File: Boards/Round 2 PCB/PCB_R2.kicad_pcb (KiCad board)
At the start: 2 copper layers, 97 x 89.5 mm, 67 parts, among them J1 Screw_Terminal_01x12, J10 Screw_Terminal_01x03, J11 Screw_Terminal_01x12, J12 Screw_Terminal_01x03, J13 Screw_Terminal_01x03, J14 Screw_Terminal_01x03, J15 Screw_Terminal_01x03, J16 Screw_Terminal_01x03, J17 Screw_Terminal_01x03, J18 Screw_Terminal_01x03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

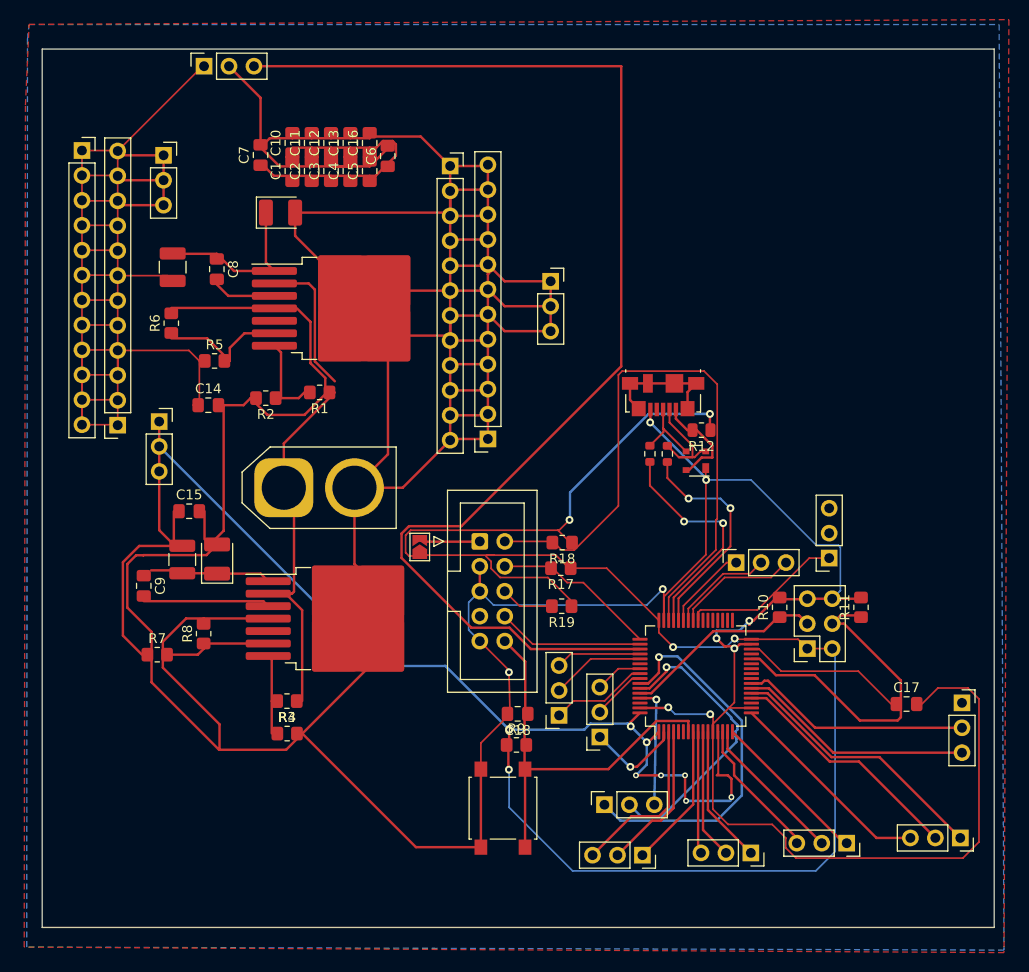
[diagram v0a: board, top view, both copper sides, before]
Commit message: ground layer test
placed all transistors, about to delete all ground connections
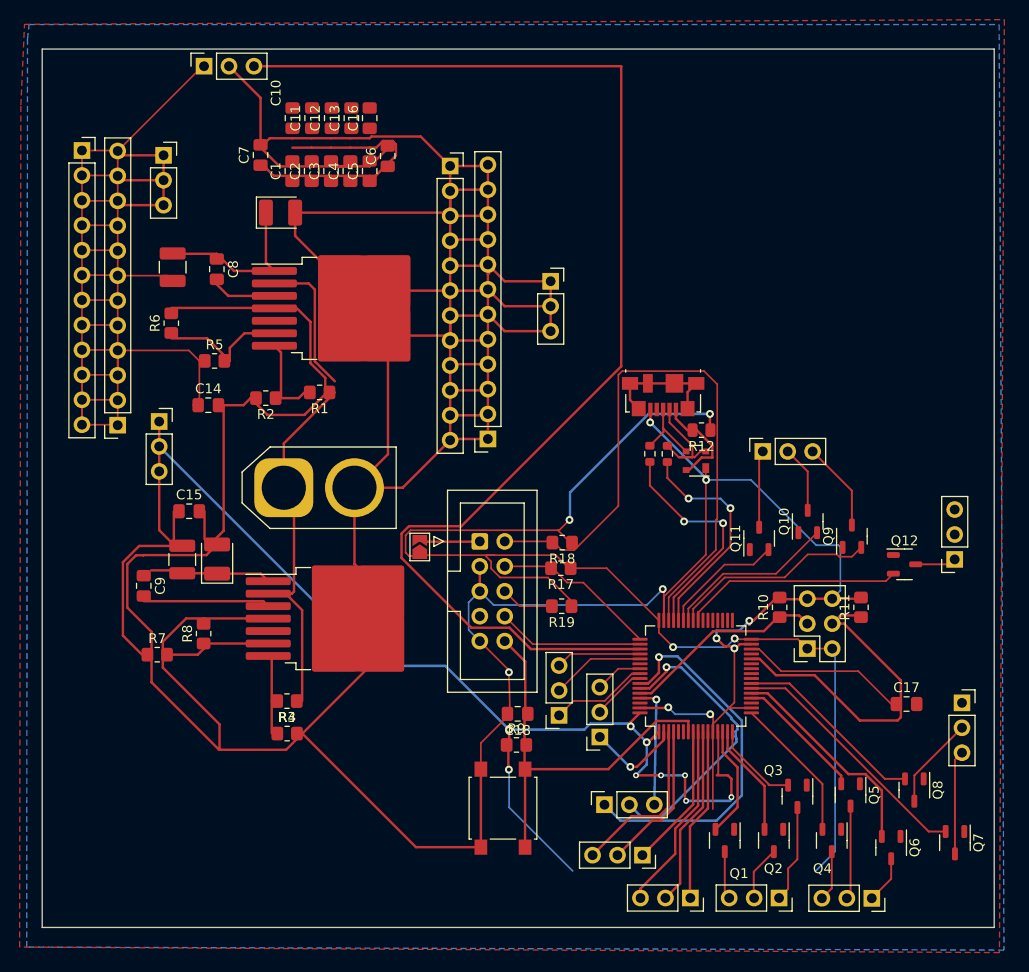
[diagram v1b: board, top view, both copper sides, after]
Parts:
- added Q1: NMOS, Package_TO_SOT_SMD:SOT-23-3, F.Cu at (121.5, 111.6)
- added Q10: NMOS, Package_TO_SOT_SMD:SOT-23-3, F.Cu at (130.0, 79.1)
- added Q11: NMOS, Package_TO_SOT_SMD:SOT-23-3, F.Cu at (125.0, 80.9)
- added Q12: NMOS, Package_TO_SOT_SMD:SOT-23-3, F.Cu at (139.9, 83.5)
- added Q2: NMOS, Package_TO_SOT_SMD:SOT-23-3, F.Cu at (126.5, 111.6)
- added Q3: NMOS, Package_TO_SOT_SMD:SOT-23-3, F.Cu at (128.9, 107.1)
- added Q4: NMOS, Package_TO_SOT_SMD:SOT-23-3, F.Cu at (132.4, 111.6)
- added Q5: NMOS, Package_TO_SOT_SMD:SOT-23-3, F.Cu at (134.4, 107.0)
- added Q6: NMOS, Package_TO_SOT_SMD:SOT-23-3, F.Cu at (138.5, 112.4)
- added Q7: NMOS, Package_TO_SOT_SMD:SOT-23-3, F.Cu at (145.0, 111.9)
- added Q8: NMOS, Package_TO_SOT_SMD:SOT-23-3, F.Cu at (140.9, 106.5)
- added Q9: NMOS, Package_TO_SOT_SMD:SOT-23-3, F.Cu at (134.5, 80.6)
- moved J15 12.8 mm to (145.0, 83.0)
- moved J10 11.6 mm to (125.4, 72.0)
- moved J13 10.9 mm to (136.5, 117.5)
- moved J12 8.87 mm to (127.1, 117.5)
- moved J19 7.69 mm to (118.0, 117.5)
- moved C13 2.53 mm to (83.5, 38.0)
- moved C12 2.53 mm to (81.5, 38.0)
- moved C11 2.53 mm to (79.5, 38.0)
- moved C10 2.53 mm to (77.5, 38.0)
- moved C16 2.53 mm to (85.4, 38.0)
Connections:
- U1 pad 14: /M0 -> /T0
- U1 pad 15: /M1 -> /T1
- U1 pad 16: /M2 -> /T2
- U1 pad 17: /M3 -> /T3
- U1 pad 20: /M4 -> /T4
- U1 pad 21: /M5 -> /T5
- U1 pad 22: /M6 -> /T6
- U1 pad 23: /M7 -> /T7
- U1 pad 40: /M11 -> /T11
- U1 pad 41: /M8 -> /T8
- U1 pad 42: /M9 -> /T9
- U1 pad 43: /M10 -> /T10
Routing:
- net GND: track 614.6 -> 562.6 mm
- net /T6: track 0.00 -> 25.8 mm
- net +3.3V: track 294.6 -> 269.8 mm
- net /T11: track 0.00 -> 24.0 mm
- net /M5: track 27.4 -> 4.84 mm
- net /T5: track 0.00 -> 22.1 mm
- net /T8: track 0.00 -> 21.1 mm
- net /T7: track 0.00 -> 19.7 mm
- net /T9: track 0.00 -> 17.5 mm
- net /M3: track 21.5 -> 5.17 mm
- net /M4: track 24.6 -> 9.54 mm
- net /M7: track 24.5 -> 9.49 mm
- net /T3: track 0.00 -> 14.9 mm
- net /M6: track 24.2 -> 10.6 mm
- net /T4: track 0.00 -> 13.2 mm
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
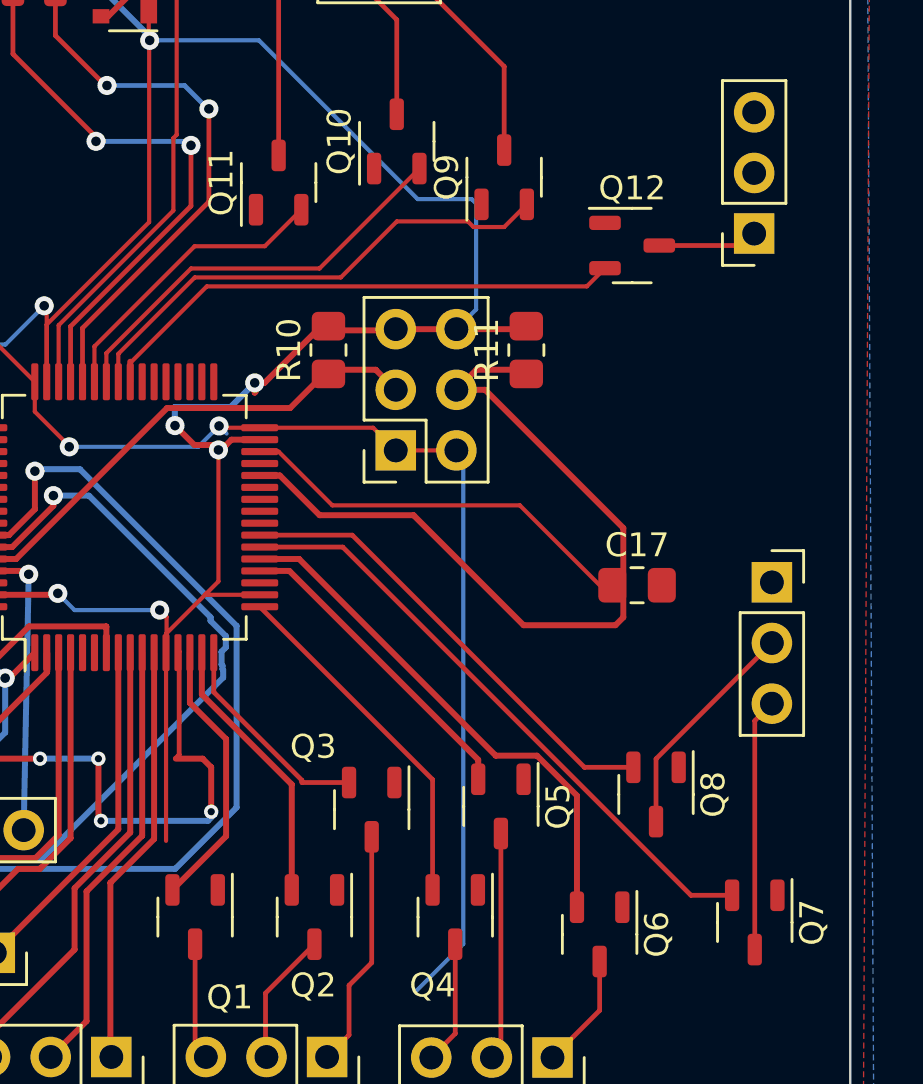
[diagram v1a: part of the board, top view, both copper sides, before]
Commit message: transistor routing
3.3V pins on all transistors are routed. Should increase net width of 3.3V bus
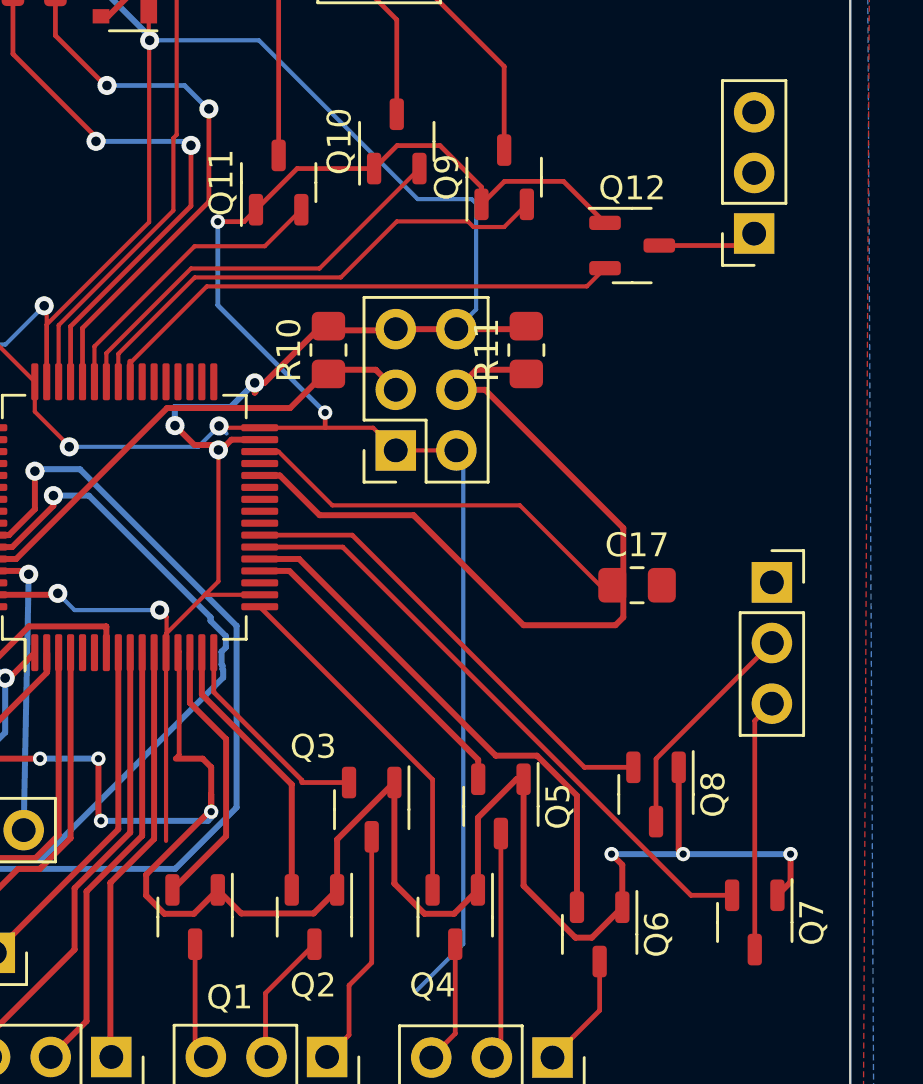
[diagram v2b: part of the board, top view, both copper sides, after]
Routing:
- net +3.3V: track 269.8 -> 360.8 mm, vias 13 -> 18

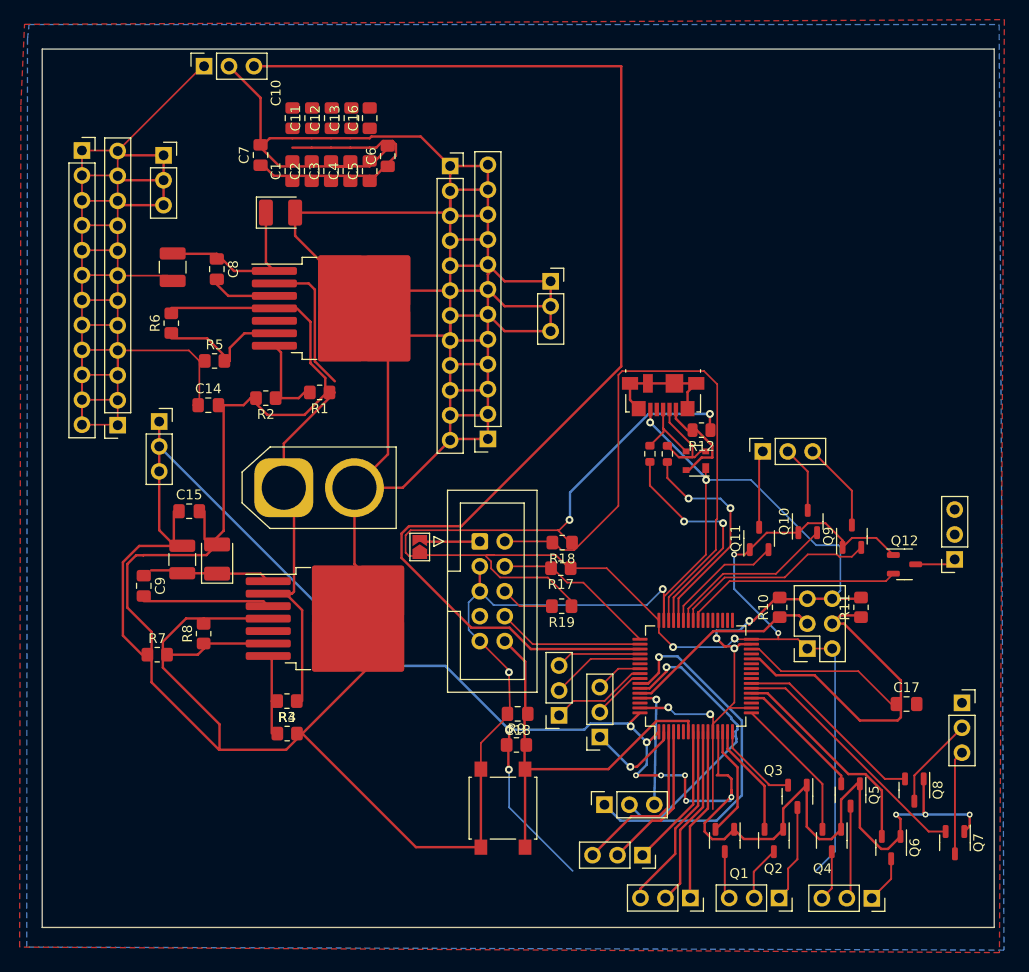
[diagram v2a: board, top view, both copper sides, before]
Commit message: error handeling
fixed all errors after adding transistors and general cleanup
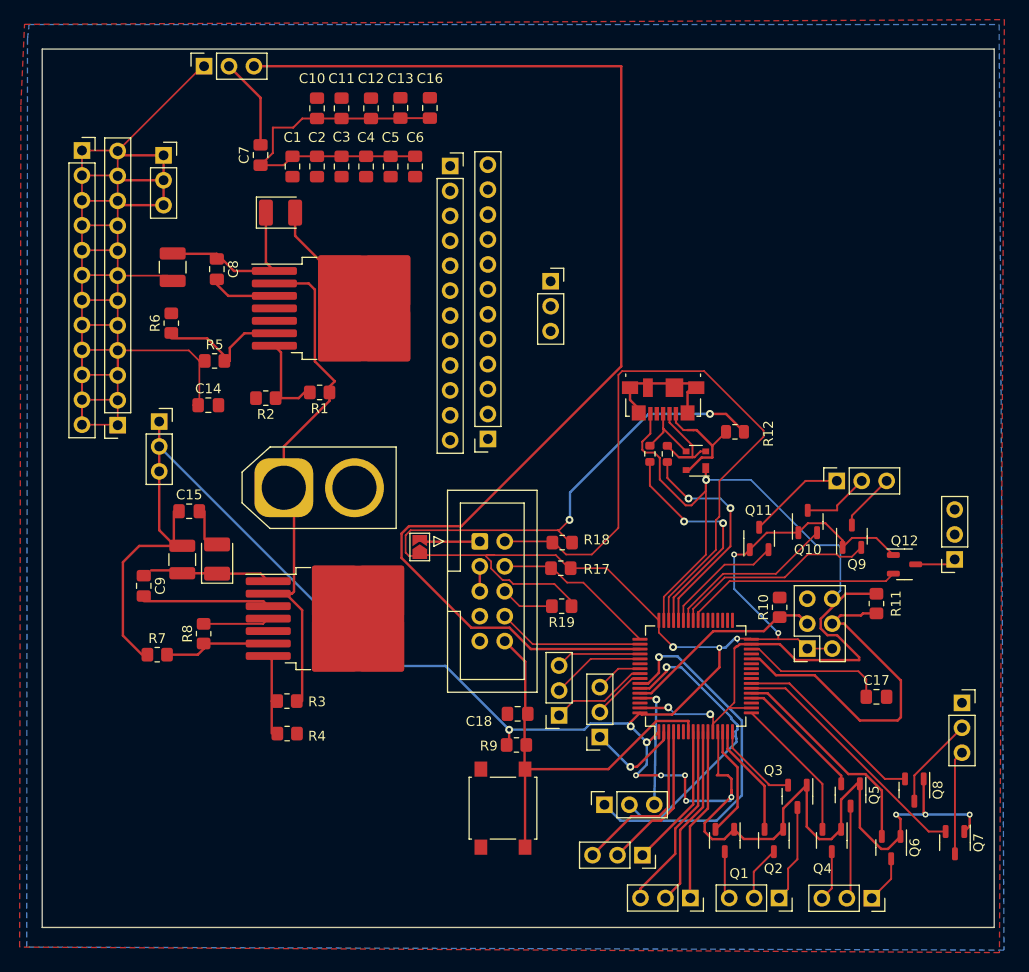
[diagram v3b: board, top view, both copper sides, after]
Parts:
- moved J10 8.11 mm to (133.0, 75.0)
- moved C16 6.22 mm to (91.5, 37.0)
- moved C13 5.11 mm to (88.5, 37.0)
- moved C12 4.12 mm to (85.5, 37.0)
- moved R12 3.41 mm to (122.6, 70.0)
- moved C11 3.16 mm to (82.5, 37.0)
- moved C17 3.15 mm to (137.0, 97.0)
- moved C6 2.98 mm to (90.0, 43.0), turned to -90 degrees
- moved C10 2.69 mm to (80.0, 37.0)
- moved C5 2.18 mm to (87.5, 43.0), turned to -90 degrees
- moved C4 1.67 mm to (85.0, 43.0), turned to -90 degrees
- moved R11 1.62 mm to (137.0, 87.5)
- moved C3 1.17 mm to (82.5, 43.0), turned to -90 degrees
- moved C2 0.72 mm to (80.0, 43.0), turned to -90 degrees
- moved C1 0.47 mm to (77.5, 43.0), turned to -90 degrees
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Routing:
- net GND: track 562.6 -> 135.7 mm, vias 9 -> 3
- net +3.3V: track 360.8 -> 336.8 mm
- net +3V3: track 27.3 -> 36.9 mm
- net /JTMS/SWDIO: track 63.9 -> 69.5 mm
- net /M8: track 9.16 -> 5.97 mm
- net /V_USB: track 10.2 -> 12.9 mm
- net /M10: track 7.88 -> 9.87 mm
- net /Vcap: track 16.6 -> 14.8 mm
- net BOOT1: track 34.4 -> 36.0 mm
- net +7.5V: track 50.3 -> 51.5 mm

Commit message: power bus width update
Updated power bus width going to each of the motors to reduce board heating
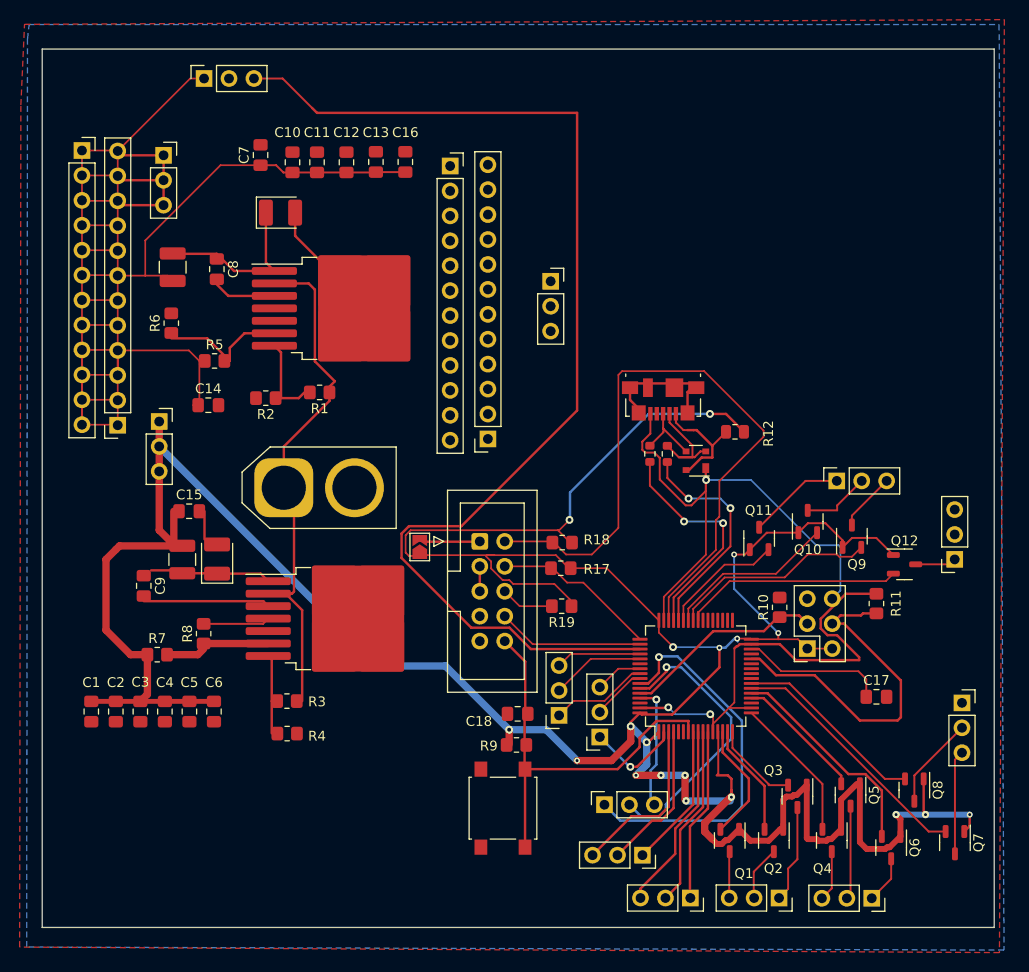
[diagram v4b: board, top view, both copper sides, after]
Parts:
- moved C1 59.2 mm to (57.0, 98.5)
- moved C2 59.2 mm to (59.5, 98.5)
- moved C3 59.2 mm to (62.0, 98.5)
- moved C4 59.2 mm to (64.5, 98.5)
- moved C5 59.2 mm to (67.0, 98.5)
- moved C6 59.2 mm to (69.5, 98.5)
- moved C10 6.04 mm to (77.5, 42.5)
- moved C11 6.04 mm to (80.0, 42.5)
- moved C12 6.04 mm to (83.0, 42.5)
- moved C13 6.04 mm to (86.0, 42.5)
- moved C16 6.04 mm to (89.0, 42.5)
- moved J9 1.25 mm to (68.5, 34.0)
- moved Q1 0.50 mm to (122.0, 111.6)
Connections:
- C1 pad 1: +3V3 -> +3.3V
- C10 pad 1: +3V3 -> +5V
- C11 pad 1: +3V3 -> +5V
- C12 pad 1: +3V3 -> +5V
- C13 pad 1: +3V3 -> +5V
- C16 pad 1: +3V3 -> +5V
- C2 pad 1: +3V3 -> +3.3V
- C3 pad 1: +3V3 -> +3.3V
- C4 pad 1: +3V3 -> +3.3V
- C5 pad 1: +3V3 -> +3.3V
- C6 pad 1: +3V3 -> +3.3V
- C7 pad 1: +3V3 -> +5V
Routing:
- net +3V3: track 36.9 -> 0.00 mm
- net +5V: track 161.8 -> 194.8 mm
- net +3.3V: track 336.8 -> 364.4 mm, vias 18 -> 19
- net /bigmotor: track 128.1 -> 118.4 mm
- net GND: track 135.7 -> 126.1 mm
- net /I2C1_SDA: track 30.2 -> 29.4 mm
- net /T0: track 11.5 -> 12.2 mm
- net /I2C1_SCL: track 38.7 -> 39.4 mm
- net /NRST: track 41.5 -> 42.1 mm
